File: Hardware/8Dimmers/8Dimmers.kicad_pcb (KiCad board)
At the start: 2 copper layers, 100 x 100 mm, 73 parts, among them J1 ISP, P10 CONN_01X02, P11 5VIN, P2 CONN_01X02, P3 CONN_01X02, P4 CONN_01X02, P5 CONN_01X02, P6 CONN_01X02, P7 CONN_01X02, P8 CONN_01X02, P9 CONN_01X02, SW1 RESET, SW2 FLASH, U1 LTV-814, U10 MOC3023M, U11 MOC3023M, U12 MOC3023M, U13 MOC3023M, U14 TRIAC_small, U15 TRIAC_small, U16 TRIAC_small, U17 TRIAC_small, U18 TRIAC_small, U19 TRIAC_small, U2 AP1117D33, U20 TRIAC_small, U21 TRIAC_small, U3 ESP-12F, U4 74HC595, U5 ULN2803A, U6 MOC3023M, U7 MOC3023M, U8 MOC3023M, U9 MOC3023M

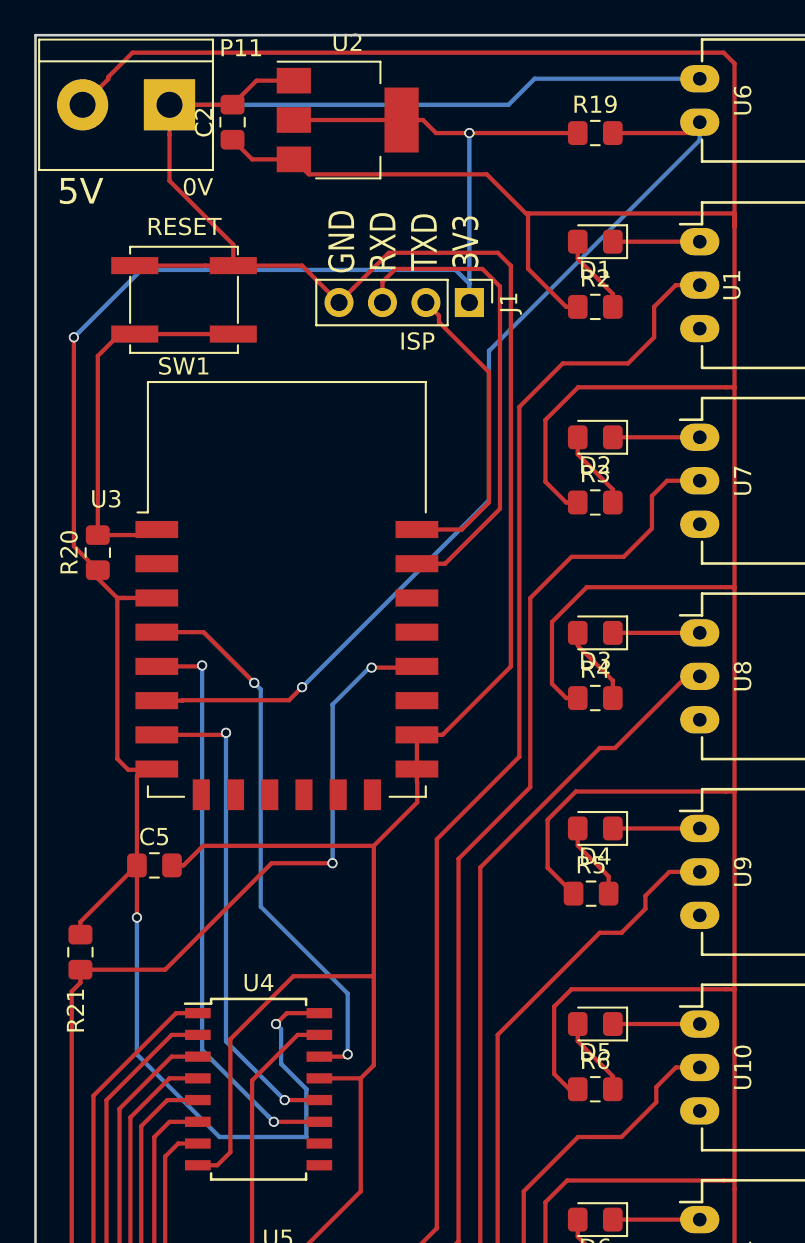
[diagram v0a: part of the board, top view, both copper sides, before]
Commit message: - Modified almost all hardware boards : They were missing a pull-up resistor on GPIO2, which made impossible to flash. - Updated baseBoard.* files
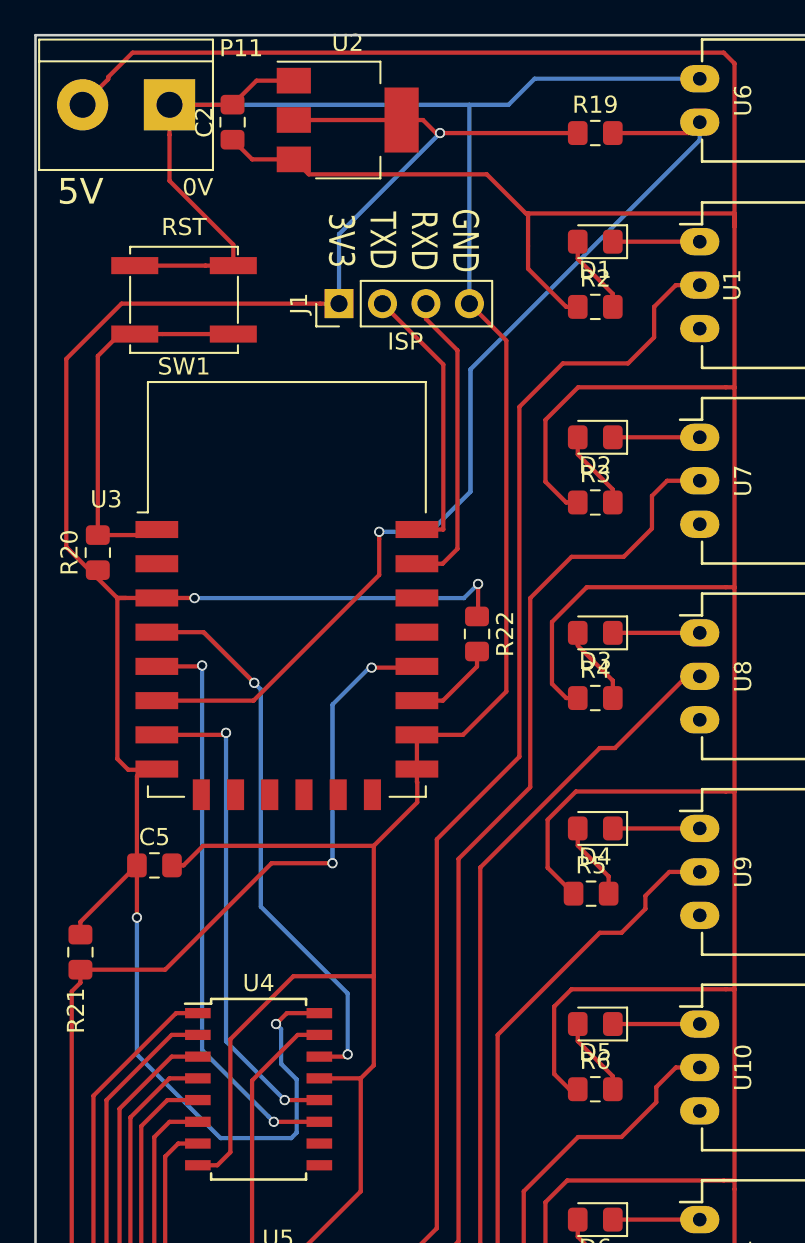
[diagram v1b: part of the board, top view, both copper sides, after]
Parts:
- added R22: 10K, Resistor_SMD:R_0805_2012Metric_Pad1.15x1.40mm_HandSolder, F.Cu at (70.8, 75.0)
- SW1: value RESET -> RST
- moved J1 7.62 mm to (62.7, 55.7), turned to 90 degrees
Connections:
- net /GPIO0 renamed Net-(R21-Pad2)
- U3 pad 10: Net-(U3-Pad10) -> (no net)
- U3 pad 11: Net-(U3-Pad11) -> (no net)
- U3 pad 12: Net-(U3-Pad12) -> (no net)
- U3 pad 13: Net-(U3-Pad13) -> (no net)
- U3 pad 14: Net-(U3-Pad14) -> (no net)
- U3 pad 19: Net-(U3-Pad19) -> (no net)
- U3 pad 2: Net-(U3-Pad2) -> (no net)
- U3 pad 20: Net-(U3-Pad20) -> (no net)
- U3 pad 9: Net-(U3-Pad9) -> (no net)
- U4 pad 10: /VCC -> (no net)
- U4 pad 9: Net-(U4-Pad9) -> (no net)
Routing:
- net /3V3: track 128.0 -> 142.1 mm, vias 4 -> 5
- net /RXD: track 28.0 -> 17.8 mm
- net GND: track 201.9 -> 194.1 mm
- net Net-(R22-Pad2): track 0.00 -> 5.22 mm
- net /TXD: track 18.1 -> 16.2 mm
- net /ZCD: track 56.8 -> 57.4 mm
